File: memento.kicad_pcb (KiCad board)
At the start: 2 copper layers, 150 x 100 mm, 5 parts, among them U1 XIAO_ESP32C3

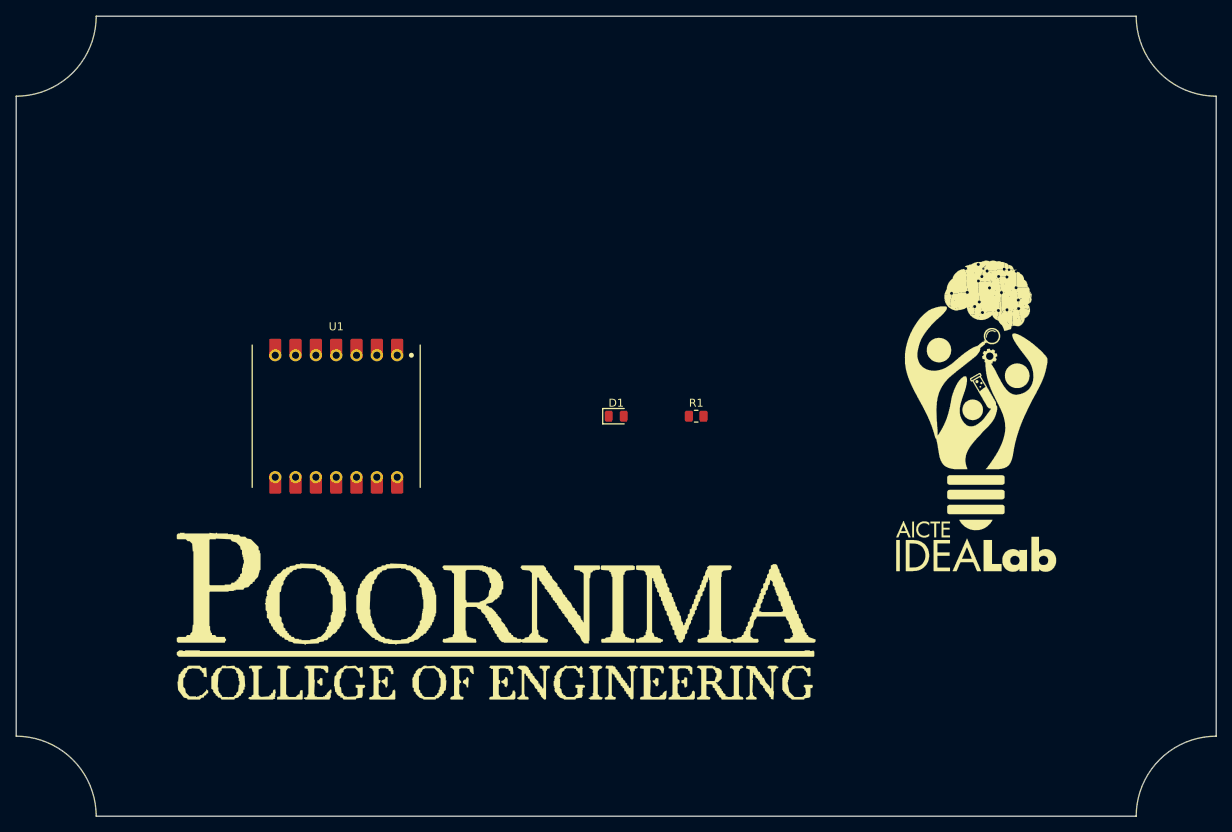
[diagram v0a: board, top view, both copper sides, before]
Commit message: Add KiBuzzard silkscreen label footprint to board
Co-Authored-By: Claude Opus 5 (1M context) <noreply@anthropic.com>
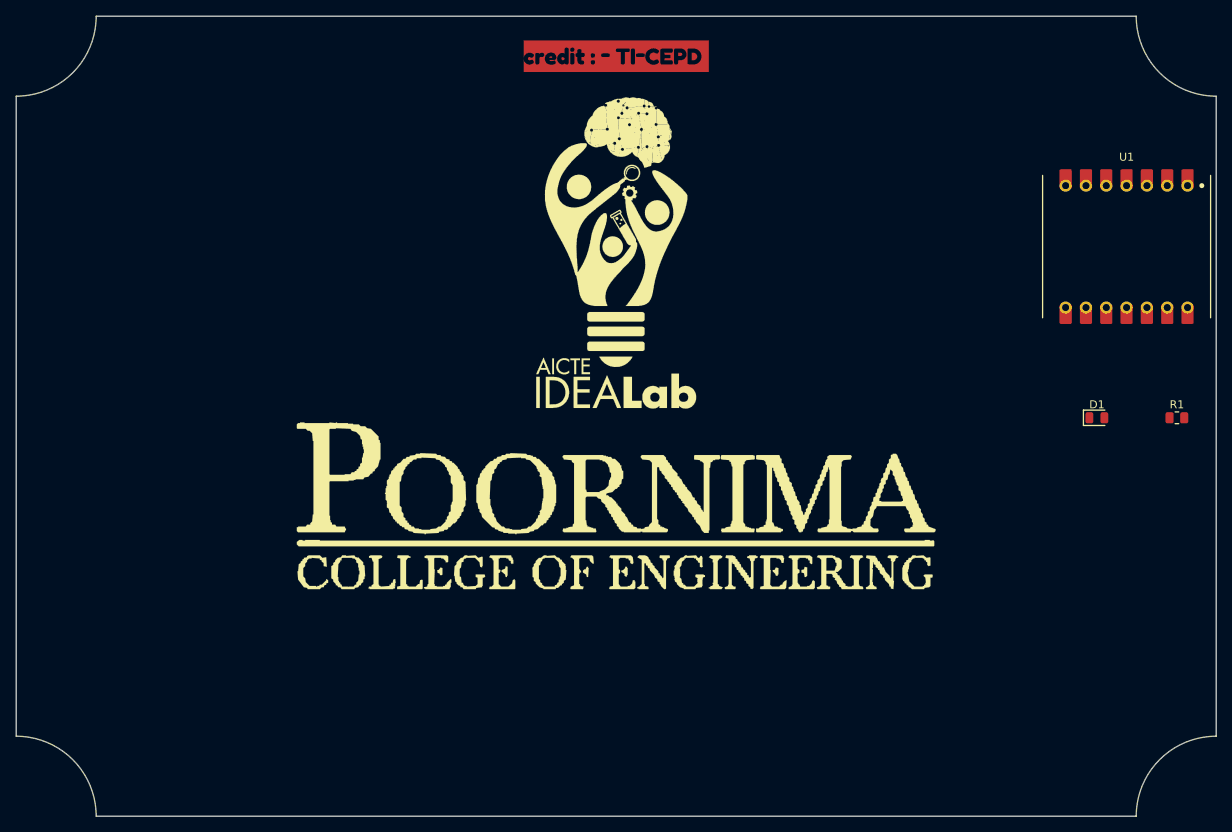
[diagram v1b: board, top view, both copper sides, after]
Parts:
- added kibuzzard-6AB60A4F: G***, kibuzzard-6AB60A4F, F.Cu at (165.0, 45.0)
- moved U1 101.0 mm to (228.8, 68.8)
- moved D1 60.1 mm to (225.1, 90.2)
- moved R1 60.1 mm to (235.1, 90.2)
- moved LOGO1 49.4 mm to (165.0, 69.6)
- moved LOGO2 20.4 mm to (165.0, 101.2)
